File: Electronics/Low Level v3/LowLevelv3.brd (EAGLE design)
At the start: 116.8 x 69.8 mm, 66 parts, among them IC2 MCP4802, K1 ORWH-SH-105D1F,000, K3 ORWH-SH-105D1F,000, Q1 16MHz, T1 2N3904, T2 2N3904, U1 284512-4, U4 MCP2515, U5 MCP2551DIL08, X3 Motor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

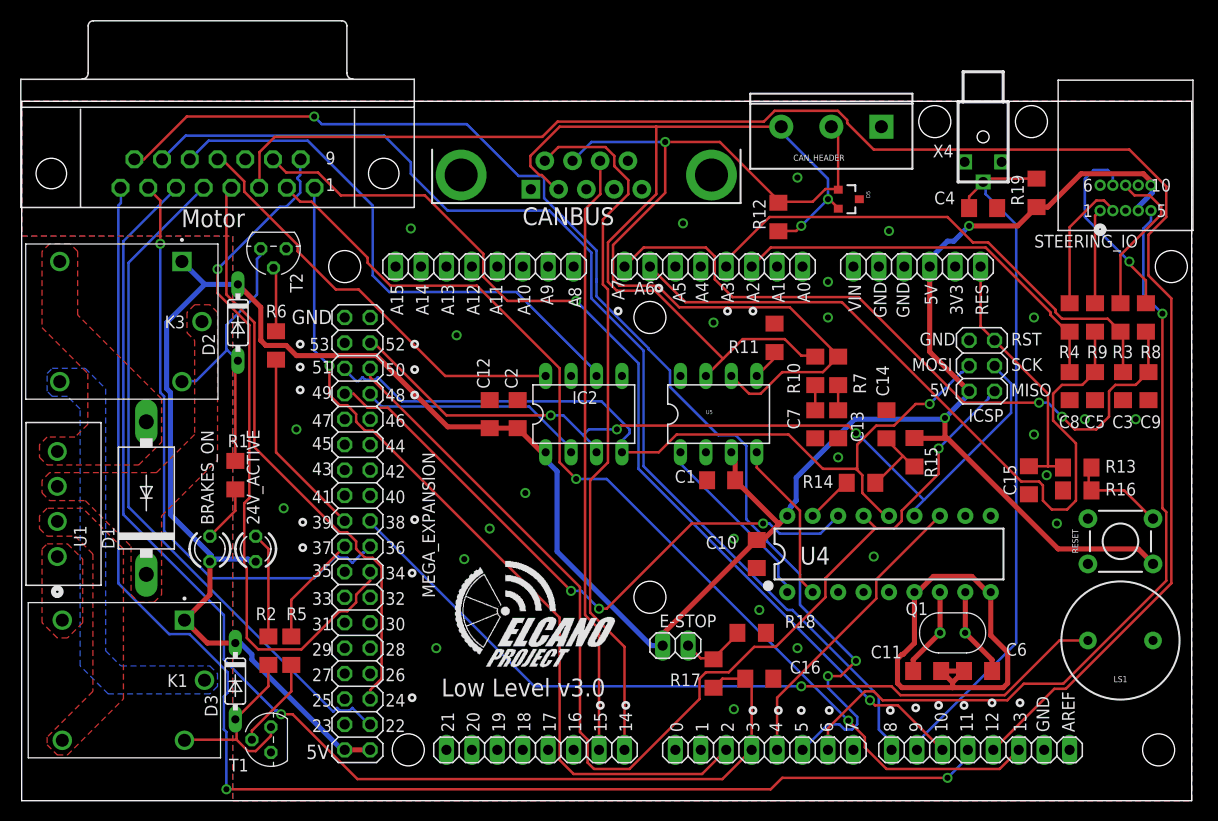
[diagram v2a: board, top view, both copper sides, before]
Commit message: corrected PCINT pin mapping
moved pretty much every interrupt pin to A8-A15, which had the secondary benefit of greatly reducing their trace length.
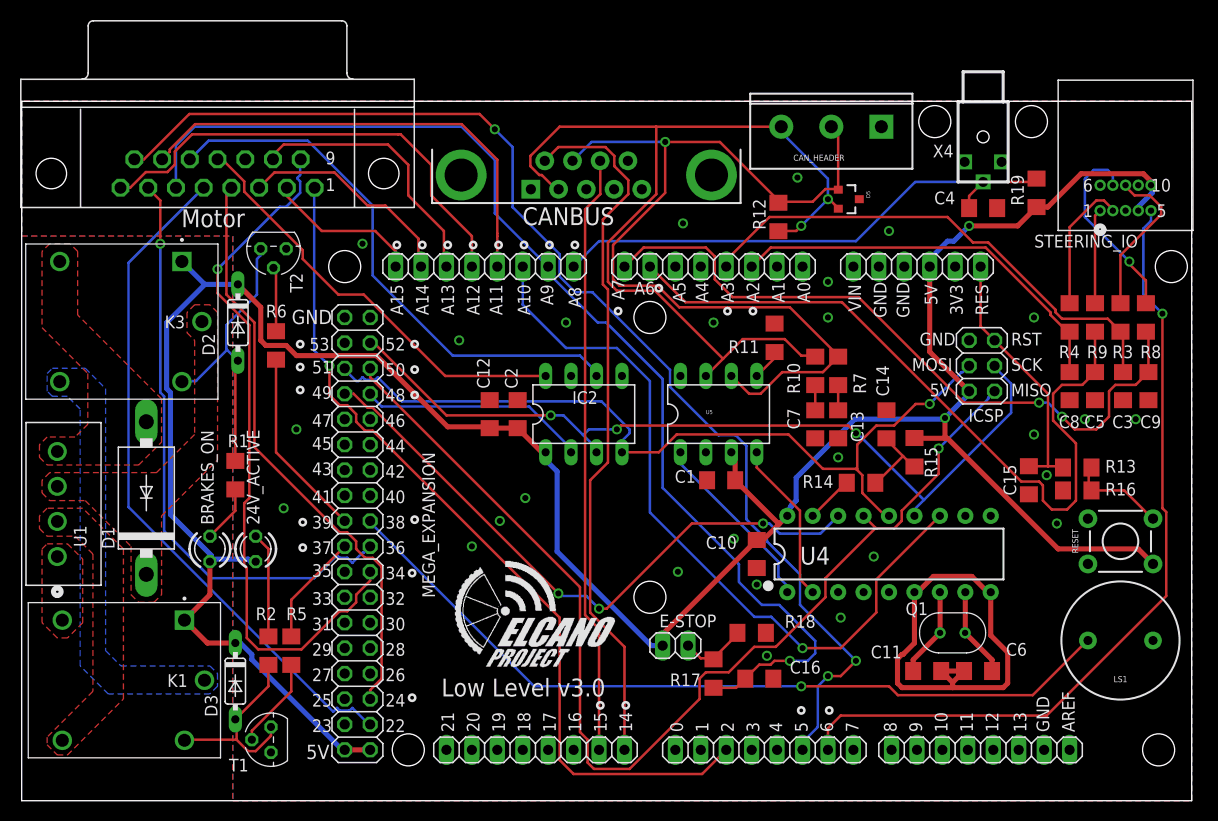
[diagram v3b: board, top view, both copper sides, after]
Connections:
- net CAN_INT: now also ADCH.6; no longer DIGITAL_0-7.5
- net EBIKECONTRL: now also ADCH.3; no longer DIGITAL_8-13.3
- net ESTOP_INT: now also ADCH.7; no longer DIGITAL_0-7.4
- net HALLPHASEA: now also ADCH.1; no longer DIGITAL_8-13.6
- net HALLPHASEB: now also ADCH.2; no longer DIGITAL_8-13.5
- net HALLPHASEC: now also ADCH.4; no longer DIGITAL_8-13.4
- net SPEEDOMETER: now also ADCH.5; no longer DIGITAL_8-13.1
- net WHEELROTATION: now also ADCH.8; no longer DIGITAL_8-13.2
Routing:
- net HALLPHASEB: track 165.1 -> 22.2 mm
- net HALLPHASEC: track 142.3 -> 47.1 mm, vias 2 -> 0
- net HALLPHASEA: track 104.3 -> 15.5 mm, vias 2 -> 0
- net EBIKECONTRL: track 98.8 -> 26.9 mm, vias 2 -> 0
- net SPEEDOMETER: track 111.7 -> 47.2 mm
- net CAN_INT: track 30.1 -> 74.8 mm, vias 0 -> 1
- net WHEELROTATION: track 70.9 -> 53.1 mm
- net ESTOP_INT: track 123.2 -> 113.8 mm
- net WATCHDOG: track 123.7 -> 120.4 mm
- net GND: vias 26 -> 27

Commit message: board cleanup, via removal, silkscreen tidying
* Changing size of almost every 'tvalue' item
* slightly tweaked trace location to allow for greater ground plane coverage
* removed redundant ground vias
* began renaming devices for clarity
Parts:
- C3, C5, C8, C9: value 1 uF -> 1uF
- R3, R4, R8, R9: value 4.7 K -> 4.7K
- moved C9 0.25 mm to (112.3, 41.4)
- moved R8 0.25 mm to (112.0, 48.3)
- moved R9 0.25 mm to (106.9, 48.3)
- renumbered IC2 to IC3_4802, K1 to PB2_12/24, K3 to PB1_BRAKE_ON, U1 to X1, U4 to IC1_2515, U5 to IC2_2551
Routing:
- net GND: track 46.0 -> 40.5 mm, vias 27 -> 22
- net RX3: track 60.0 -> 61.9 mm
- net L_SENSE: track 40.3 -> 42.0 mm
- net STEER_SERVO_PWM: track 81.2 -> 82.6 mm
- net MISO: track 111.1 -> 112.4 mm
- net MOSI: track 82.9 -> 84.2 mm
- net R_SENSE: track 50.8 -> 52.0 mm
- net BRAKE_PWM: track 86.4 -> 87.5 mm
- net L_RET: track 9.46 -> 10.2 mm
- net CANL: track 93.4 -> 92.9 mm
- net L_RTN_GND: track 74.6 -> 75.1 mm
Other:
- board text added: "L/H/G"

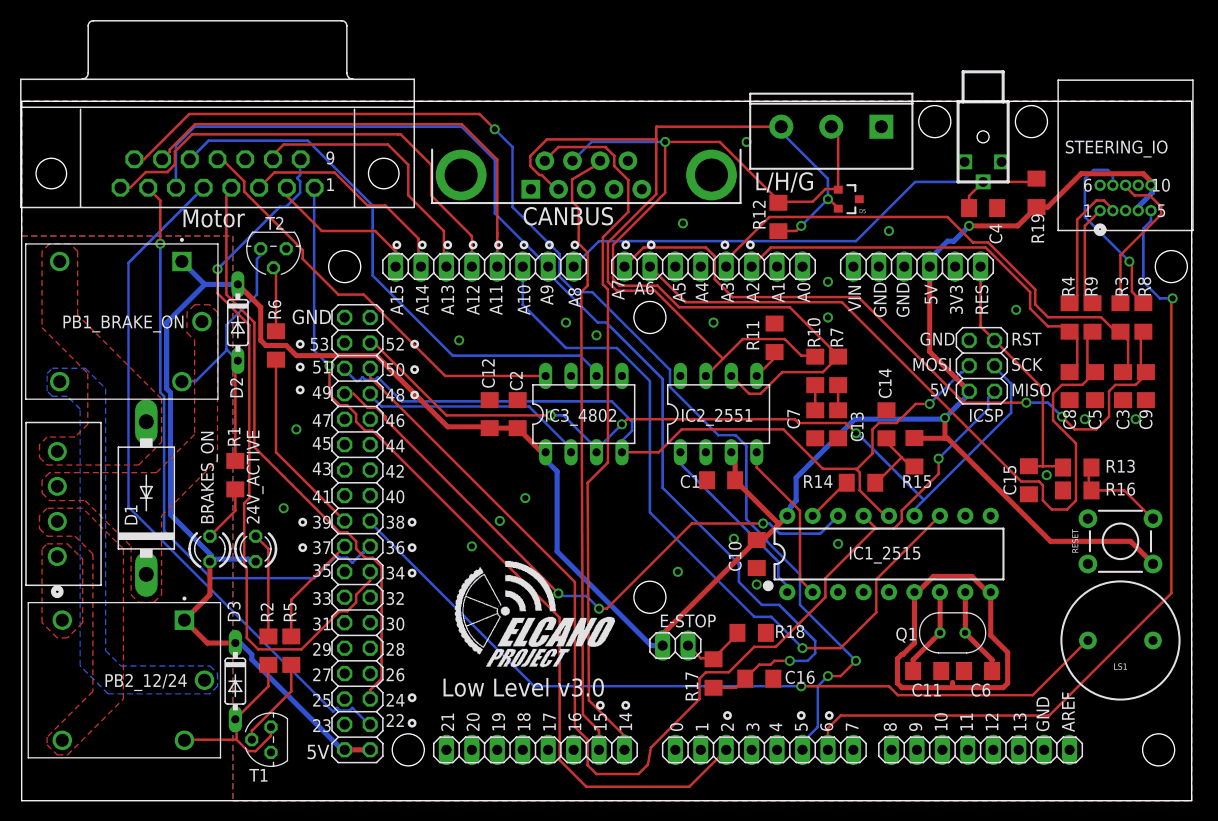
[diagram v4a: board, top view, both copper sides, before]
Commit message: lots of renaming and slight position changes
* renamed caps and resistors to make populating the board a little easier
* moved silk around to try and be a little more coherent
* slight copper adjustments to get more ground fill
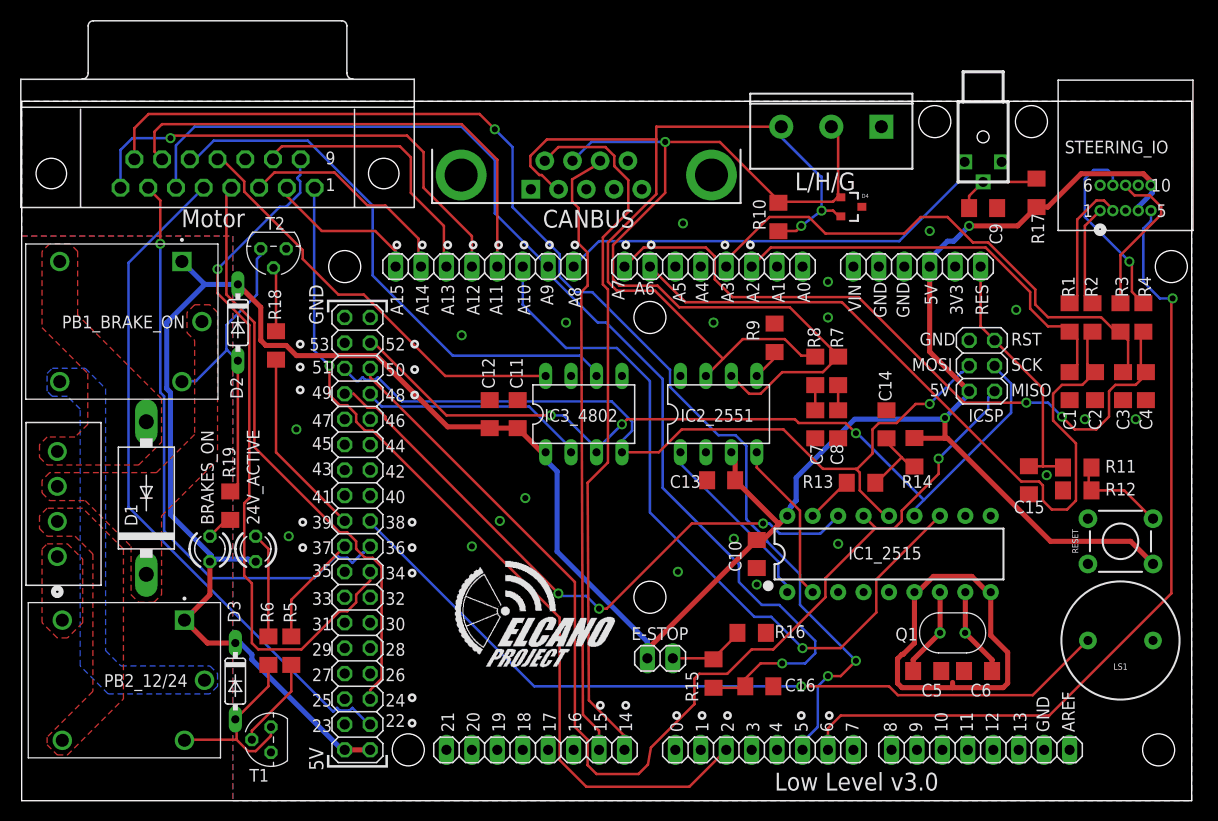
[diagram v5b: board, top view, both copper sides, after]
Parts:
- removed D5: PESD1CAN, elcanoParts:SPARKFUN-DISCRETESEMI_SOT23-3
- added D4: PESD1CAN, elcanoParts:SPARKFUN-DISCRETESEMI_SOT23-3
- C1, C2: value 0.1uF -> 1uF
- C11: value 33pF -> 0.1uF
- C13: value 560pF -> 0.1uF
- C4: value 1 uF -> 1uF
- C5: value 1uF -> 33pF
- C8: value 1uF -> 560pF
- C9: value 1uF -> 1 uF
- R1, R2: value 1K -> 4.7K
- R10: value 100 -> 120
- R11: value 4.7K -> 10k
- R12: value 120 -> 10k
- R13, R18: value 10k -> 1K
- R14: value 1K -> 20K
- R15: value 20K -> 10k
- R17: value 10k -> 4.7K
- R19: value 4.7K -> 1K
- R8: value 4.7K -> 100
- moved R2 88.8 mm to (106.9, 48.3)
- moved R19 86.4 mm to (20.8, 29.5), turned to 270 degrees
- moved R1 84.8 mm to (104.6, 48.3), turned to 90 degrees
- moved R17 57.8 mm to (101.3, 60.7)
- moved C2 57.7 mm to (107.2, 41.4), turned to 270 degrees
- moved R18 55.5 mm to (25.4, 45.5), turned to 90 degrees
- moved C11 48.3 mm to (49.5, 38.6), turned to 90 degrees
- moved R12 40.5 mm to (105.4, 31.0), turned to 180 degrees
- moved C1 36.0 mm to (104.6, 41.4), turned to 270 degrees
- moved R16 35.5 mm to (72.9, 16.8), turned to 0 degrees
- moved R8 33.2 mm to (79.2, 42.9)
- moved C5 33.0 mm to (90.4, 13.0), turned to 0 degrees
- moved R11 32.9 mm to (105.4, 33.3), turned to 0 degrees
- moved R9 31.8 mm to (75.2, 46.2)
- moved R6 30.5 mm to (24.6, 15.0)
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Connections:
- net 5V: now also C11.1, C13.1, R14.1, R17.1; no longer C1.1, C2.1, R15.1, R19.1
- net BRAKE_ON: now also R18.1; no longer R6.1
- net CANH: now also D4.1, R10.2; no longer D5.1, R12.2
- net CANL: now also D4.2, R10.1, R8.2; no longer D5.2, R10.2, R12.1
- net ESTOP_INT: now also R15.1; no longer R17.1
- net GND: now also D4.3, R12.2, R9.2; no longer D5.3, R11.2, R18.2
- net L_RET: now also R2.2; no longer R9.2
- net L_RTN_GND: now also C2.1, R2.1; no longer C5.1, R9.1
- net L_SENSE: now also C1.1, R1.1; no longer C8.1, R4.1
- net L_STR: now also R1.2; no longer R4.2
- net N$1: now also R11.2, R12.1; no longer R13.2, R16.1
- net N$10: now also C8.1; no longer C13.1
- net N$12: now also R19.1; no longer R1.1
- net N$13: now also R19.2; no longer R1.2
- net N$14: now also R9.1; no longer R11.1
- net N$3: now also R6.1; no longer R2.1
- net N$4: now also R13.2; no longer R15.2
- net N$6: now also R6.2; no longer R2.2
- net N$7: now also R18.2; no longer R6.2
- net N$8: now also R15.2, R16.1; no longer R17.2, R18.1
- net N$9: now also R8.1; no longer R10.1
- net OSC2: now also C5.1; no longer C11.1
- net RESET: now also R11.1; no longer R13.1
- net RS: now also R13.1; no longer R14.1
- net R_RET: now also R4.2; no longer R8.2
- net R_RTN_GND: now also C4.1, R4.1; no longer C9.1, R8.1
- net WHEELROTATION: now also C9.1, R17.2; no longer C4.1, R19.2
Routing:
- net N$12: track 29.0 -> 32.3 mm
- net N$13: track 5.73 -> 2.71 mm
- net SPEEDOMETER: track 47.2 -> 49.8 mm
- net 5V: track 266.3 -> 268.1 mm
- net WATCHDOG: track 120.4 -> 122.2 mm
- net HALLPHASEC: track 47.1 -> 48.7 mm, vias 0 -> 1
- net R_SENSE: track 52.0 -> 53.3 mm
- net N$8: track 6.76 -> 7.75 mm
- net CANH: track 91.9 -> 92.7 mm
- net GND: vias 22 -> 20

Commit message: Checkpoint for first PCB order
* few minor routing changes
* extended a 1x8 to a 1x10 because some Mega boards have two more pins on one header.
* added partial bill of materials
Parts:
- DIGITAL_8-13: device pinhead:1X08 -> pinhead:1X10
- moved DIGITAL_8-13 2.79 mm to (98.6, 5.08)
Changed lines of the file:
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@@
 <attribute name="VALUE" x="114.3" y="42.164" size="0.635" layer="27" ratio="10" rot="R270"/>
 </element>
-<element name="DIGITAL_8-13" library="pinhead" library_urn="urn:adsk.eagle:library:325" package="1X08" package3d_urn="urn:adsk.eagle:package:22409/2" value="Digital 8-13" x="95.758" y="5.08" smashed="yes"/>
+<element name="DIGITAL_8-13" library="pinhead" library_urn="urn:adsk.eagle:library:325" package="1X10" package3d_urn="urn:adsk.eagle:package:22406/2" value="Digital 8-13" x="98.552" y="5.08" smashed="yes"/>
 <element name="IC1_2515" library="SparkFun-IC-Comms" library_urn="urn:adsk.eagle:library:521" package="DIP18" package3d_urn="urn:adsk.eagle:package:38724/1" value=" MCP2515" x="86.614" y="24.638" smashed="yes">
 <attribute name="NAME" x="82.55" y="24.0919" size="1.27" layer="25" ratio="10"/>
@@
 <wire x1="81.534" y1="60.529" x2="81.804" y2="60.259" width="0.254" layer="1"/>
 <wire x1="80.899" y1="67.31" x2="80.852" y2="67.31" width="0.254" layer="1"/>
-<wire x1="81.026" y1="59.817" x2="75.692" y2="59.817" width="0.254" layer="1"/>
+<wire x1="81.026" y1="59.817" x2="75.946" y2="59.817" width="0.254" layer="1"/>
+<wire x1="75.946" y1="59.817" x2="75.692" y2="59.817" width="0.254" layer="1"/>
 <wire x1="75.692" y1="59.817" x2="75.565" y2="59.817" width="0.254" layer="1"/>
 <wire x1="81.417509375" y1="60.208509375" x2="81.026" y2="59.817" width="0.254" layer="1"/>
@@
 <wire x1="56.896" y1="65.786" x2="55.118" y2="64.008" width="0.254" layer="16"/>
 <wire x1="64.262" y1="65.786" x2="56.896" y2="65.786" width="0.254" layer="16"/>
-<wire x1="69.723" y1="65.786" x2="64.262" y2="65.786" width="0.254" layer="1"/>
-<wire x1="75.692" y1="59.817" x2="69.723" y2="65.786" width="0.254" layer="1"/>
+<wire x1="69.723" y1="66.04" x2="64.516" y2="66.04" width="0.254" layer="1"/>
+<wire x1="64.516" y1="66.04" x2="64.262" y2="65.786" width="0.254" layer="1"/>
+<wire x1="75.946" y1="59.817" x2="69.723" y2="66.04" width="0.254" layer="1"/>
 <wire x1="55.118" y1="64.008" x2="55.008" y2="63.904" width="0.254" layer="16"/>
 <wire x1="75.692" y1="59.817" x2="75.565" y2="59.715" width="0.254" layer="1"/>
@@
 <wire x1="50.8" y1="63.373" x2="51.689" y2="62.484" width="0.254" layer="1"/>
 <wire x1="50.8" y1="64.389" x2="50.8" y2="63.373" width="0.254" layer="1"/>
-<wire x1="52.451" y1="66.04" x2="50.8" y2="64.389" width="0.254" layer="1"/>
-<wire x1="75.852" y1="67.31" x2="63.373" y2="67.31" width="0.254" layer="1"/>
-<wire x1="63.373" y1="66.04" x2="52.451" y2="66.04" width="0.254" layer="1"/>
+<wire x1="53.213" y1="66.802" x2="50.8" y2="64.389" width="0.254" layer="1"/>
+<wire x1="75.852" y1="67.31" x2="75.344" y2="66.802" width="0.254" layer="1"/>
+<wire x1="75.344" y1="66.802" x2="63.373" y2="66.802" width="0.254" layer="1"/>
+<wire x1="63.373" y1="66.802" x2="53.213" y2="66.802" width="0.254" layer="1"/>
 <wire x1="53.594" y1="61.087" x2="53.618" y2="61.064" width="0.254" layer="1"/>
 <wire x1="63.246" y1="50.927" x2="70.0405" y2="44.1325" width="0.254" layer="1"/>
@@
 <wire x1="58.547" y1="55.753" x2="58.547" y2="51.816" width="0.254" layer="1"/>
 <wire x1="63.373" y1="60.579" x2="58.547" y2="55.753" width="0.254" layer="1"/>
-<wire x1="63.373" y1="67.31" x2="63.373" y2="66.04" width="0.254" layer="1"/>
-<wire x1="63.373" y1="66.04" x2="63.373" y2="60.579" width="0.254" layer="1"/>
+<wire x1="63.373" y1="66.802" x2="63.373" y2="60.579" width="0.254" layer="1"/>
 <via x="79.883" y="58.928" extent="1-16" drill="0.6096"/>
 <via x="77.851" y="57.404" extent="1-16" drill="0.6096"/>

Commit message: swapped 0.2uF for 0.1uF, updated BoM
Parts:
- C15, C16: value 200nF -> 1uF
- C9: value 1 uF -> 1uF
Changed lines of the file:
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@@
 <attribute name="VALUE" x="114.3" y="42.164" size="0.635" layer="27" ratio="10" rot="R270"/>
 </element>
-<element name="C9" library="resistor" library_urn="urn:adsk.eagle:library:348" package="C1206" package3d_urn="urn:adsk.eagle:package:23618/2" value="1 uF" x="96.012" y="59.182" smashed="yes">
+<element name="C9" library="resistor" library_urn="urn:adsk.eagle:library:348" package="C1206" package3d_urn="urn:adsk.eagle:package:23618/2" value="1uF" x="96.012" y="59.182" smashed="yes">
 <attribute name="NAME" x="96.647" y="57.658" size="1.27" layer="25" ratio="10" rot="R270"/>
 <attribute name="VALUE" x="98.044" y="57.658" size="0.635" layer="27" ratio="10" rot="R270"/>
@@
 <attribute name="SF_SKU" value="COM-07950" x="109.728" y="16.002" size="1.778" layer="27" rot="R180" display="off"/>
 </element>
-<element name="C15" library="resistor" library_urn="urn:adsk.eagle:library:348" package="C1206" package3d_urn="urn:adsk.eagle:package:23618/2" value="200nF" x="100.584" y="32.004" smashed="yes" rot="R270">
+<element name="C15" library="resistor" library_urn="urn:adsk.eagle:library:348" package="C1206" package3d_urn="urn:adsk.eagle:package:23618/2" value="1uF" x="100.584" y="32.004" smashed="yes" rot="R270">
 <attribute name="NAME" x="99.06" y="28.702" size="1.27" layer="25"/>
 <attribute name="VALUE" x="102.108" y="28.448" size="0.635" layer="27" rot="R180"/>
@@
 <attribute name="VALUE" x="72.898" y="14.986" size="0.635" layer="27"/>
 </element>
-<element name="C16" library="resistor" library_urn="urn:adsk.eagle:library:348" package="C1206" package3d_urn="urn:adsk.eagle:package:23618/2" value="200nF" x="73.66" y="11.43" smashed="yes">
+<element name="C16" library="resistor" library_urn="urn:adsk.eagle:library:348" package="C1206" package3d_urn="urn:adsk.eagle:package:23618/2" value="1uF" x="73.66" y="11.43" smashed="yes">
 <attribute name="NAME" x="76.2" y="10.922" size="1.27" layer="25"/>
 <attribute name="VALUE" x="72.39" y="9.652" size="0.635" layer="27"/>
